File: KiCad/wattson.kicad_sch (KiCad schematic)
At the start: 24 parts, among them SW1 Keypad 1, SW10 Plug, SW11 On/Off, SW2 Keypad 2, SW3 Keypad 3, SW4 Keypad 4, SW5 Keypad 5, SW6 Keypad 0, SW7 Keypad 6, SW8 Keypad 7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

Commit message: add vibration motors
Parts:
- added Q1, Q2: NPN, symbol Simulation_SPICE:NPN
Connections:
- net +5V: now also Q1.1 (C), Q2.1 (C)
- net at U2.1 (GPB0): no longer R6.1
- net at U2.2 (GPB1): now also Q1.2 (B); no longer SW9.1
- net at U2.3 (GPB2): now also Q2.2 (B); no longer SW10.1
- net at U2.4 (GPB3): now also R6.1; no longer R3.2
- net at U2.5 (GPB4): now also SW9.1; no longer R4.2
- net at U2.6 (GPB5): now also SW10.1
- net at U2.7 (GPB6): now also R3.2
- net at U2.8 (GPB7): now also R4.2
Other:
- note added: "Vibration Motor"

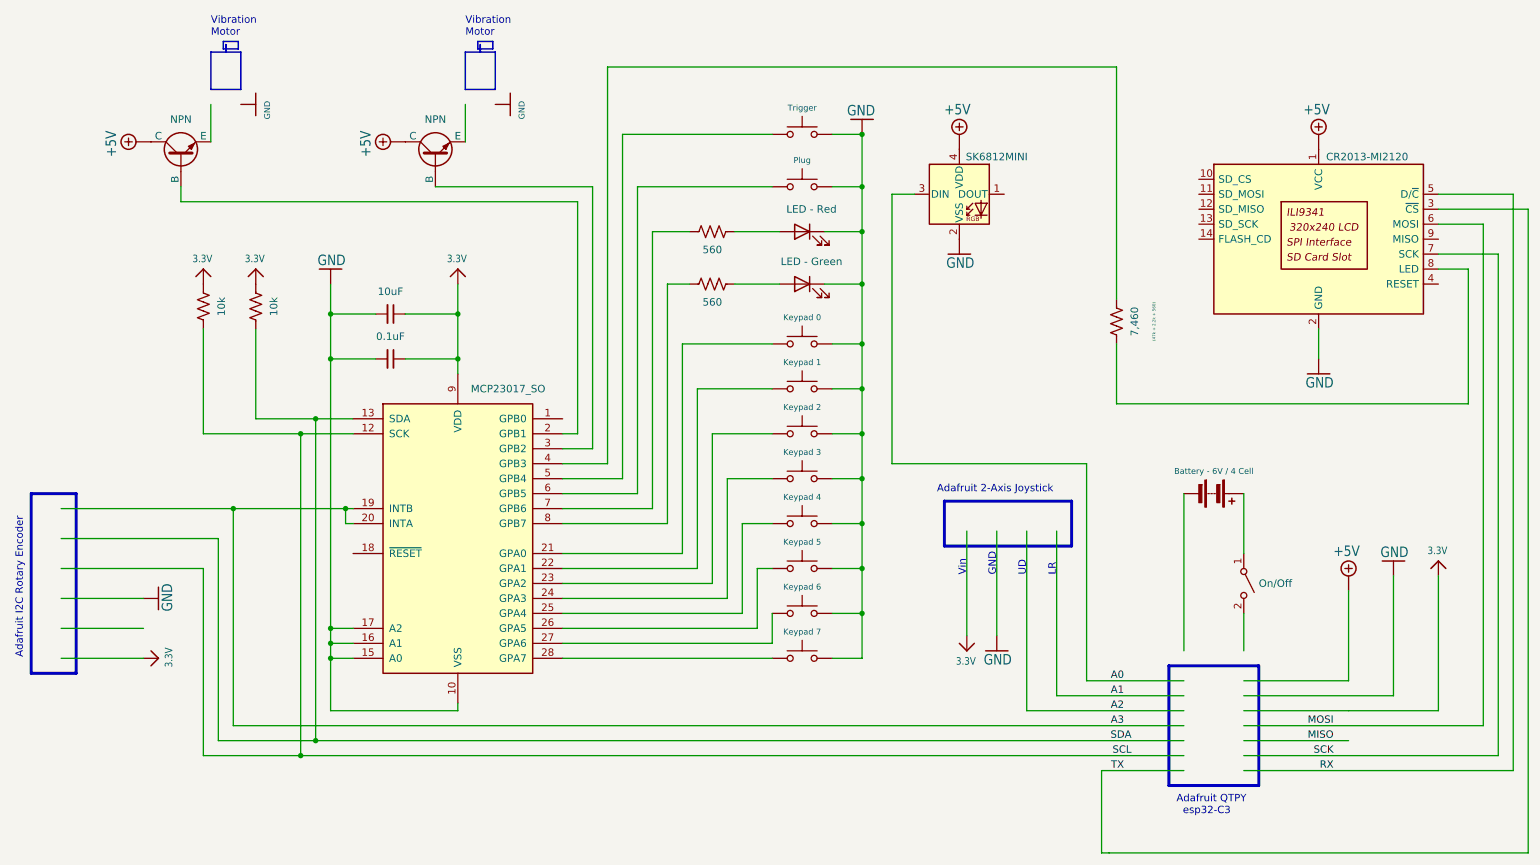
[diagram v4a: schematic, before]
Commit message: use waterfall interrupts, update schemas
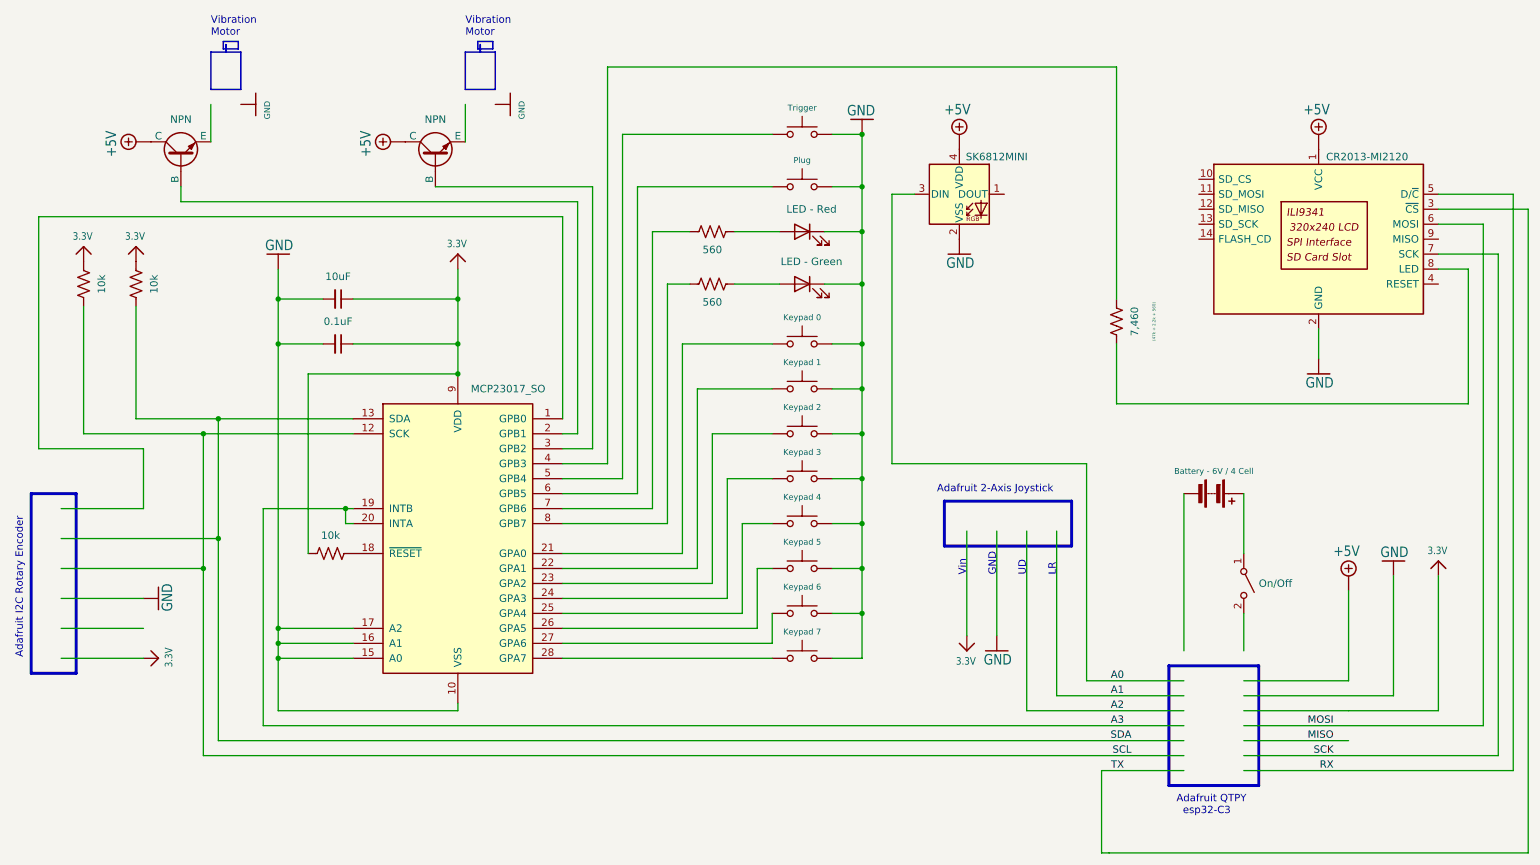
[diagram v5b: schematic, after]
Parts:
- added R5: 10k, symbol Device:R_US
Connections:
- net 3.3V: now also R5.1
- net at U2.18 (~{RESET}): now also R5.2

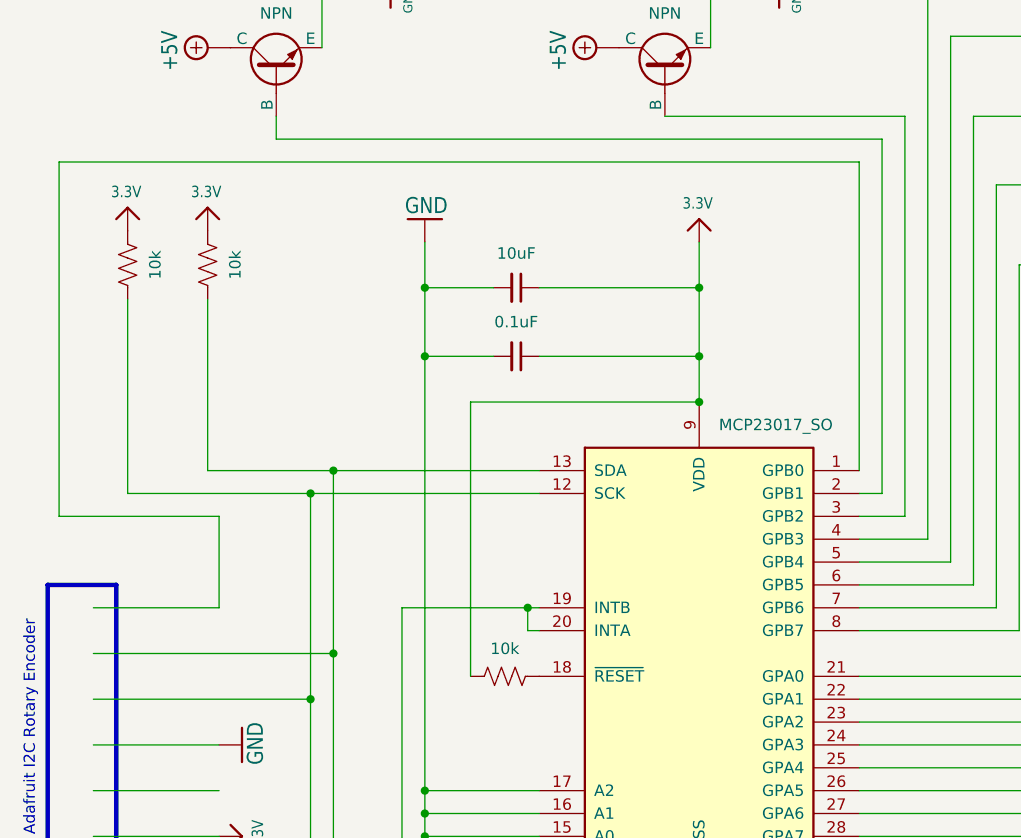
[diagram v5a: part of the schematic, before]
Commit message: use waterfall interrupts, update schemas
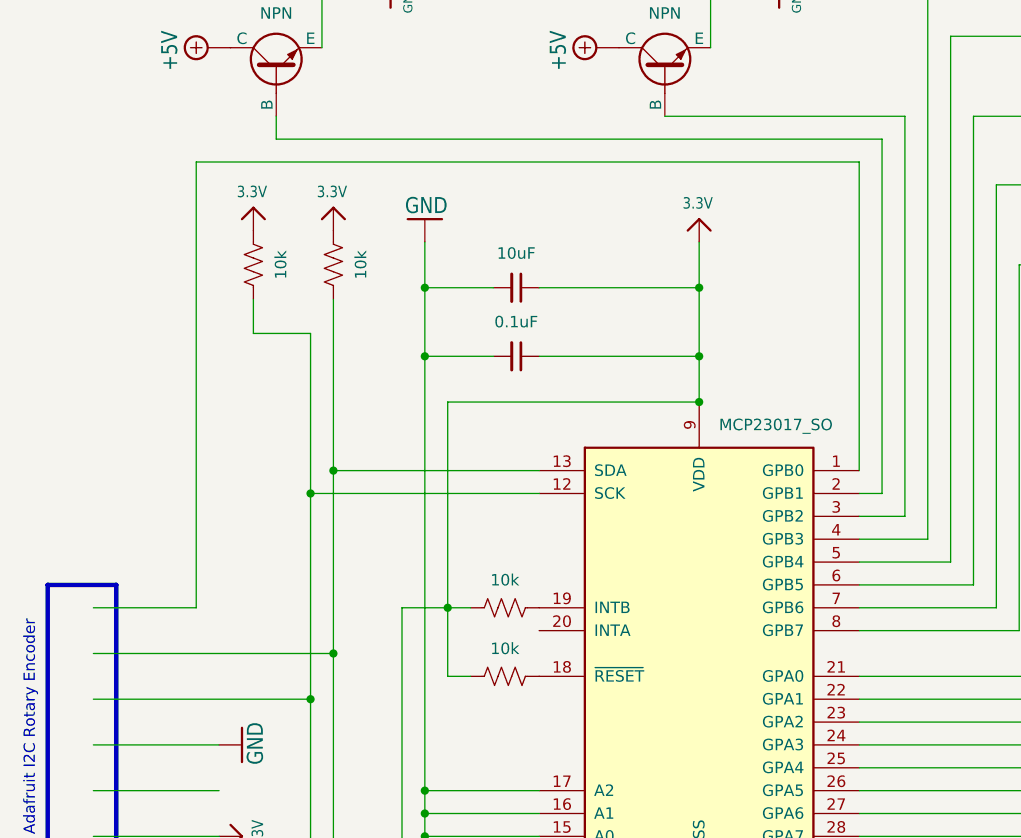
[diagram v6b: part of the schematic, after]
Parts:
- added R7: 10k, symbol Device:R_US
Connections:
- net 3.3V: now also R7.1
- net A3: no longer names the net of U2.19 (INTB)
- net A3: now also R7.2; no longer U2.20 (INTA)
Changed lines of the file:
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@@
   (junction (at 62.23 68.58) (diameter 0) (color 0 0 0 0)
   )
-  (junction (at 73.66 96.52) (diameter 0) (color 0 0 0 0)
-  )
   (junction (at 161.29 58.42) (diameter 0) (color 0 0 0 0)
   )
@@
   )
   (junction (at 92.71 73.66) (diameter 0) (color 0 0 0 0)
+  )
+  (junction (at 64.77 96.52) (diameter 0) (color 0 0 0 0)
   )
   (junction (at 49.53 106.68) (diameter 0) (color 0 0 0 0)
@@
     (stroke (width 0) (type default))
   )
-  (wire (pts (xy 67.31 104.14) (xy 67.31 73.66))
+  (wire (pts (xy 64.77 104.14) (xy 64.77 96.52))
     (stroke (width 0) (type default))
   )
@@
     (stroke (width 0) (type default))
   )
-  (wire (pts (xy 21.59 46.99) (xy 110.49 46.99))
+  (wire (pts (xy 36.83 46.99) (xy 110.49 46.99))
     (stroke (width 0) (type default))
   )
@@
     (stroke (width 0) (type default))
   )
-  (wire (pts (xy 38.1 62.23) (xy 38.1 81.28))
+  (wire (pts (xy 52.07 62.23) (xy 52.07 81.28))
     (stroke (width 0) (type default))
   )
@@
     (stroke (width 0) (type default))
   )
-  (wire (pts (xy 25.4 96.52) (xy 39.37 96.52))
+  (wire (pts (xy 25.4 96.52) (xy 36.83 96.52))
     (stroke (width 0) (type default))
   )
@@
     (stroke (width 0) (type default))
   )
-  (wire (pts (xy 59.69 96.52) (xy 73.66 96.52))
-    (stroke (width 0) (type default))
-  )
   (wire (pts (xy 128.27 99.06) (xy 110.49 99.06))
     (stroke (width 0) (type default))
@@
     (stroke (width 0) (type default))
   )
-  (wire (pts (xy 73.66 96.52) (xy 74.93 96.52))
-    (stroke (width 0) (type default))
-  )
   (wire (pts (xy 62.23 130.81) (xy 92.71 130.81))
     (stroke (width 0) (type default))
@@
     (stroke (width 0) (type default))
   )
-  (wire (pts (xy 39.37 86.36) (xy 21.59 86.36))
-    (stroke (width 0) (type default))
-  )
   (wire (pts (xy 271.78 43.18) (xy 259.08 43.18))
     (stroke (width 0.1524) (type solid))
@@
     (stroke (width 0) (type default))
   )
+  (wire (pts (xy 64.77 96.52) (xy 67.31 96.52))
+    (stroke (width 0) (type default))
+  )
   (wire (pts (xy 204.47 78.74) (xy 204.47 68.58))
     (stroke (width 0) (type default))
   )
+  (wire (pts (xy 49.53 66.04) (xy 49.53 83.82))
+    (stroke (width 0) (type default))
+  )
+  (wire (pts (xy 64.77 96.52) (xy 64.77 73.66))
+    (stroke (width 0) (type default))
+  )
   (wire (pts (xy 118.11 88.9) (xy 110.49 88.9))
     (stroke (width 0) (type default))
@@
     (stroke (width 0) (type default))
   )
-  (wire (pts (xy 67.31 73.66) (xy 92.71 73.66))
+  (wire (pts (xy 64.77 73.66) (xy 92.71 73.66))
     (stroke (width 0) (type default))
   )
@@
   )
   (wire (pts (xy 204.47 21.59) (xy 118.11 21.59))
-    (stroke (width 0) (type default))
-  )
-  (wire (pts (xy 73.66 99.06) (xy 73.66 96.52))
     (stroke (width 0) (type default))
   )
@@
     (stroke (width 0) (type default))
   )
-  (wire (pts (xy 29.21 62.23) (xy 29.21 83.82))
+  (wire (pts (xy 43.18 62.23) (xy 43.18 66.04))
     (stroke (width 0) (type default))
   )
@@
     (stroke (width 0.1524) (type solid))
   )
+  (wire (pts (xy 59.69 96.52) (xy 64.77 96.52))
+    (stroke (width 0) (type default))
+  )
   (wire (pts (xy 143.51 116.84) (xy 143.51 106.68))
     (stroke (width 0) (type default))
@@
     (stroke (width 0) (type default))
   )
-  (wire (pts (xy 38.1 81.28) (xy 52.07 81.28))
-    (stroke (width 0) (type default))
-  )
   (wire (pts (xy 52.07 81.28) (xy 74.93 81.28))
     (stroke (width 0) (type default))
@@
     (stroke (width 0) (type default))
   )
-  (wire (pts (xy 29.21 83.82) (xy 49.53 83.82))
+  (wire (pts (xy 43.18 66.04) (xy 49.53 66.04))
     (stroke (width 0) (type default))
   )
@@
     (stroke (width 0.1524) (type solid))
   )
-  (wire (pts (xy 39.37 96.52) (xy 39.37 86.36))
+  (wire (pts (xy 36.83 46.99) (xy 36.83 96.52))
     (stroke (width 0) (type default))
   )
@@
     (stroke (width 0.1524) (type solid))
   )
+  (wire (pts (xy 64.77 104.14) (xy 67.31 104.14))
+    (stroke (width 0) (type default))
+  )
   (wire (pts (xy 259.08 130.81) (xy 243.84 130.81))
     (stroke (width 0) (type default))
@@
     (stroke (width 0) (type default))
   )
-  (wire (pts (xy 74.93 99.06) (xy 73.66 99.06))
-    (stroke (width 0) (type default))
-  )
   (wire (pts (xy 135.89 109.22) (xy 135.89 83.82))
     (stroke (width 0) (type default))
@@
   )
   (wire (pts (xy 62.23 119.38) (xy 62.23 121.92))
-    (stroke (width 0) (type default))
-  )
-  (wire (pts (xy 21.59 86.36) (xy 21.59 46.99))
     (stroke (width 0) (type default))
   )
@@
     )
   )
-  (symbol (lib_id "Device:R_US") (at 38.1 58.42 0) (unit 1)
-    (in_bom yes) (on_board yes) (dnp no)
-    (property "Reference" "R1" (at 44.45 58.42 90)
-      (effects (font (size 1.27 1.27)) hide)
-    )
-    (property "Value" "10k" (at 41.91 58.42 90)
+  (symbol (lib_id "Device:R_US") (at 52.07 58.42 0) (unit 1)
+    (in_bom yes) (on_board yes) (dnp no)
+    (property "Reference" "R1" (at 58.42 58.42 90)
+      (effects (font (size 1.27 1.27)) hide)
+    )
+    (property "Value" "10k" (at 55.88 58.42 90)
       (effects (font (size 1.27 1.27)) (justify bottom))
     )
-    (property "Footprint" "" (at 39.116 58.674 90)
-      (effects (font (size 1.27 1.27)) hide)
-    )
-    (property "Datasheet" "~" (at 38.1 58.42 0)
+    (property "Footprint" "" (at 53.086 58.674 90)
+      (effects (font (size 1.27 1.27)) hide)
+    )
+    (property "Datasheet" "~" (at 52.07 58.42 0)
       (effects (font (size 1.27 1.27)) hide)
     )
@@
     )
   )
-  (symbol (lib_id "Adafruit QT Py ESP32-C3-eagle-import:3.3V") (at 38.1 52.07 0) (mirror y) (unit 1)
-    (in_bom yes) (on_board yes) (dnp no)
-    (property "Reference" "#U$10" (at 38.1 52.07 0)
-      (effects (font (size 1.27 1.27)) hide)
-    )
-    (property "Value" "3.3V" (at 39.624 51.054 0)
+  (symbol (lib_id "Adafruit QT Py ESP32-C3-eagle-import:3.3V") (at 52.07 52.07 0) (mirror y) (unit 1)
+    (in_bom yes) (on_board yes) (dnp no)
+    (property "Reference" "#U$10" (at 52.07 52.07 0)
+      (effects (font (size 1.27 1.27)) hide)
+    )
+    (property "Value" "3.3V" (at 53.594 51.054 0)
       (effects (font (size 1.27 1.0795)) (justify left bottom))
     )
-    (property "Footprint" "" (at 38.1 52.07 0)
-      (effects (font (size 1.27 1.27)) hide)
-    )
-    (property "Datasheet" "" (at 38.1 52.07 0)
+    (property "Footprint" "" (at 52.07 52.07 0)
+      (effects (font (size 1.27 1.27)) hide)
+    )
+    (property "Datasheet" "" (at 52.07 52.07 0)
       (effects (font (size 1.27 1.27)) hide)
     )
@@
     )
   )
-  (symbol (lib_id "Adafruit QT Py ESP32-C3-eagle-import:3.3V") (at 29.21 52.07 0) (mirror y) (unit 1)
-    (in_bom yes) (on_board yes) (dnp no)
-    (property "Reference" "#U$10" (at 29.21 52.07 0)
-      (effects (font (size 1.27 1.27)) hide)
-    )
-    (property "Value" "3.3V" (at 30.734 51.054 0)
+  (symbol (lib_id "Adafruit QT Py ESP32-C3-eagle-import:3.3V") (at 43.18 52.07 0) (mirror y) (unit 1)
+    (in_bom yes) (on_board yes) (dnp no)
+    (property "Reference" "#U$10" (at 43.18 52.07 0)
+      (effects (font (size 1.27 1.27)) hide)
+    )
+    (property "Value" "3.3V" (at 44.704 51.054 0)
       (effects (font (size 1.27 1.0795)) (justify left bottom))
     )
-    (property "Footprint" "" (at 29.21 52.07 0)
-      (effects (font (size 1.27 1.27)) hide)
-    )
-    (property "Datasheet" "" (at 29.21 52.07 0)
+    (property "Footprint" "" (at 43.18 52.07 0)
+      (effects (font (size 1.27 1.27)) hide)
+    )
+    (property "Datasheet" "" (at 43.18 52.07 0)
       (effects (font (size 1.27 1.27)) hide)
     )
@@
     )
   )
-  (symbol (lib_id "Device:R_US") (at 29.21 58.42 0) (unit 1)
-    (in_bom yes) (on_board yes) (dnp no)
-    (property "Reference" "R2" (at 35.56 58.42 90)
-      (effects (font (size 1.27 1.27)) hide)
-    )
-    (property "Value" "10k" (at 33.02 58.42 90)
+  (symbol (lib_id "Device:R_US") (at 43.18 58.42 0) (unit 1)
+    (in_bom yes) (on_board yes) (dnp no)
+    (property "Reference" "R2" (at 49.53 58.42 90)
+      (effects (font (size 1.27 1.27)) hide)
+    )
+    (property "Value" "10k" (at 46.99 58.42 90)
       (effects (font (size 1.27 1.27)) (justify bottom))
     )
-    (property "Footprint" "" (at 30.226 58.674 90)
-      (effects (font (size 1.27 1.27)) hide)
-    )
-    (property "Datasheet" "~" (at 29.21 58.42 0)
+    (property "Footprint" "" (at 44.196 58.674 90)
+      (effects (font (size 1.27 1.27)) hide)
+    )
+    (property "Datasheet" "~" (at 43.18 58.42 0)
       (effects (font (size 1.27 1.27)) hide)
     )
@@
         )
       )
+    )
+  )
+  (symbol (lib_id "Device:R_US") (at 71.12 96.52 90) (unit 1)
+    (in_bom yes) (on_board yes) (dnp no)
+    (property "Reference" "R7" (at 71.12 90.17 90)
+      (effects (font (size 1.27 1.27)) hide)
+    )
+    (property "Value" "10k" (at 71.12 92.71 90)
+      (effects (font (size 1.27 1.27)) (justify bottom))
+    )
+    (property "Footprint" "" (at 71.374 95.504 90)
+      (effects (font (size 1.27 1.27)) hide)
+    )
+    (property "Datasheet" "~" (at 71.12 96.52 0)
+      (effects (font (size 1.27 1.27)) hide)
+    )
+    (pin "1")
+    (pin "2")
+    (instances
+      (project "wattson"
+        (path "/eff6c10b-1292-455c-9802-f747f2a9f123"
+          (reference "R7") (unit 1)
+        )
+      )
